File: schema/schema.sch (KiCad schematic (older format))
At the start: 10 parts, among them J1 Conn_01x04_Male, J2 Conn_01x04_Male, J3 Conn_01x05_Male

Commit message: Update PCB
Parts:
- C2, C4: footprint Capacitors_THT:CP_Radial_D5.0mm_P2.50mm -> Capacitor_THT:CP_Radial_D8.0mm_P5.00mm
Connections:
- wire segments 81 -> 75
- no-connect marks 0 -> 62
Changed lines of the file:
@@
 $EndDescr
-$Comp
-L schema-rescue:ARDUINO_MEGA-shield_arduino-test-rescue SH1
-U 1 1 5E01C684
-P 3250 3800
-F 0 "SH1" H 3262 6593 60  0000 C CNN
-F 1 "ARDUINO_MEGA" H 3262 6487 60  0000 C CNN
-F 2 "SHIELD_ARDUINO:ARDUINO_MEGA_2560_R3_ELL" H 2300 4100 60  0001 C CNN
-F 3 "http://arduino.cc/en/Main/ArduinoBoardMega2560" H 3262 6381 60  0000 C CNN
-	1    3250 3800
-	1    0    0    -1
-$EndComp
 $Comp
 L Driver_Motor:Pololu_Breakout_A4988 A1
@@
 	7000 1550 7200 1550
 Wire Wire Line
-	7200 1850 7000 1850
-Wire Wire Line
-	7000 1950 7200 1950
-Wire Wire Line
 	7200 2050 7000 2050
-Wire Wire Line
-	7000 2250 7200 2250
-Wire Wire Line
-	7200 2350 7000 2350
 Wire Wire Line
 	7000 2450 7200 2450
@@
 	4700 2500 4800 2400
 Wire Wire Line
-	4400 2500 4425 2500
-Connection ~ 4425 2500
-Wire Wire Line
-	4425 2500 4700 2500
-Wire Wire Line
-	4400 2300 4425 2300
-Connection ~ 4425 2300
-Wire Wire Line
-	4425 2300 4700 2300
-Wire Wire Line
-	4400 2200 4425 2200
-Connection ~ 4425 2200
-Wire Wire Line
-	4425 2200 4700 2200
-Wire Wire Line
-	4400 2100 4425 2100
-Connection ~ 4425 2100
-Wire Wire Line
-	4425 2100 4700 2100
-Wire Wire Line
-	4400 2000 4425 2000
-Connection ~ 4425 2000
-Wire Wire Line
-	4425 2000 4700 2000
-Wire Wire Line
-	4400 1800 4425 1800
-Connection ~ 4425 1800
-Wire Wire Line
 	4425 1800 4700 1800
-Wire Wire Line
-	4400 1900 4425 1900
-Connection ~ 4425 1900
 Wire Wire Line
 	4425 1900 4700 1900
@@
 	0    -1   -1   0
 $EndComp
-Connection ~ 2100 2200
 Wire Wire Line
 	1550 2000 2100 2000
@@
 F 0 "C2" H 8388 1446 50  0000 L CNN
 F 1 "100u" H 8388 1355 50  0000 L CNN
-F 2 "Capacitors_THT:CP_Radial_D5.0mm_P2.50mm" H 8300 1400 50  0001 C CNN
+F 2 "Capacitor_THT:CP_Radial_D8.0mm_P5.00mm" H 8300 1400 50  0001 C CNN
 F 3 "~" H 8300 1400 50  0001 C CNN
 	1    8300 1400
@@
 F 0 "C4" H 8488 4196 50  0000 L CNN
 F 1 "100u" H 8488 4105 50  0000 L CNN
-F 2 "Capacitors_THT:CP_Radial_D5.0mm_P2.50mm" H 8400 4150 50  0001 C CNN
+F 2 "Capacitor_THT:CP_Radial_D8.0mm_P5.00mm" H 8400 4150 50  0001 C CNN
 F 3 "~" H 8400 4150 50  0001 C CNN
 	1    8400 4150
@@
 Wire Wire Line
 	4650 5550 5850 5550
+NoConn ~ 2100 4300
+NoConn ~ 2100 4400
+NoConn ~ 2100 5075
+NoConn ~ 2100 4875
+NoConn ~ 2100 4775
+NoConn ~ 2100 4675
+NoConn ~ 2100 4575
+NoConn ~ 2100 5175
+NoConn ~ 2100 5275
+NoConn ~ 2100 5375
+NoConn ~ 2100 5475
+NoConn ~ 2100 5575
+NoConn ~ 2100 5675
+NoConn ~ 2100 5775
+NoConn ~ 2100 5975
+NoConn ~ 2100 6075
+NoConn ~ 2100 6175
+NoConn ~ 2100 6275
+NoConn ~ 4425 6150
+NoConn ~ 4425 6050
+NoConn ~ 4425 5850
+NoConn ~ 4425 5750
+NoConn ~ 4425 5650
+NoConn ~ 4425 5550
+NoConn ~ 4425 5450
+NoConn ~ 4425 5250
+NoConn ~ 4425 5150
+NoConn ~ 4425 5050
+NoConn ~ 4425 4950
+NoConn ~ 4425 4850
+NoConn ~ 4425 4750
+NoConn ~ 4425 4650
+NoConn ~ 4425 4550
+NoConn ~ 4425 4400
+NoConn ~ 4425 4300
+NoConn ~ 4425 4100
+NoConn ~ 4425 4000
+NoConn ~ 4425 3900
+NoConn ~ 4425 3800
+NoConn ~ 4425 3700
+NoConn ~ 4425 3600
+NoConn ~ 4425 3500
+NoConn ~ 4425 3400
+NoConn ~ 4425 3200
+NoConn ~ 4425 3100
+NoConn ~ 4425 2900
+NoConn ~ 4425 2800
+NoConn ~ 4425 2700
+NoConn ~ 4425 2600
+Wire Wire Line
+	4425 1700 4450 1700
+NoConn ~ 4425 1600
+NoConn ~ 4425 1500
+NoConn ~ 4425 1400
+Wire Wire Line
+	4425 2200 4700 2200
+Wire Wire Line
+	4425 2000 4700 2000
+Wire Wire Line
+	4425 2100 4700 2100
+Connection ~ 2100 2200
+Wire Wire Line
+	4425 2300 4700 2300
+Wire Wire Line
+	4425 2500 4700 2500
+Wire Wire Line
+	4425 3000 4650 3000
 Wire Wire Line
 	4400 3000 4425 3000
 Connection ~ 4425 3000
-Wire Wire Line
-	4425 3000 4650 3000
+$Comp
+L schema-rescue:ARDUINO_MEGA-shield_arduino-test-rescue SH1
+U 1 1 5E01C684
+P 3250 3800
+F 0 "SH1" H 3262 6593 60  0000 C CNN
+F 1 "ARDUINO_MEGA" H 3262 6487 60  0000 C CNN
+F 2 "SHIELD_ARDUINO:ARDUINO_MEGA_2560_R3_ELL" H 2300 4100 60  0001 C CNN
+F 3 "http://arduino.cc/en/Main/ArduinoBoardMega2560" H 3262 6381 60  0000 C CNN
+	1    3250 3800
+	1    0    0    -1
+$EndComp
+NoConn ~ 2100 1700
+NoConn ~ 2100 1800
+NoConn ~ 2100 1900
+NoConn ~ 2100 2700
+NoConn ~ 2100 2800
+NoConn ~ 2100 2900
+NoConn ~ 2100 3000
+NoConn ~ 2100 3100
+NoConn ~ 2100 3200
+NoConn ~ 7200 1650
+Wire Wire Line
+	7000 2250 7200 2250
+Wire Wire Line
+	7000 2350 7200 2350
+Wire Wire Line
+	7200 1850 7000 1850
+Wire Wire Line
+	7200 1950 7000 1950
 Wire Bus Line
 	4800 1700 4800 3850

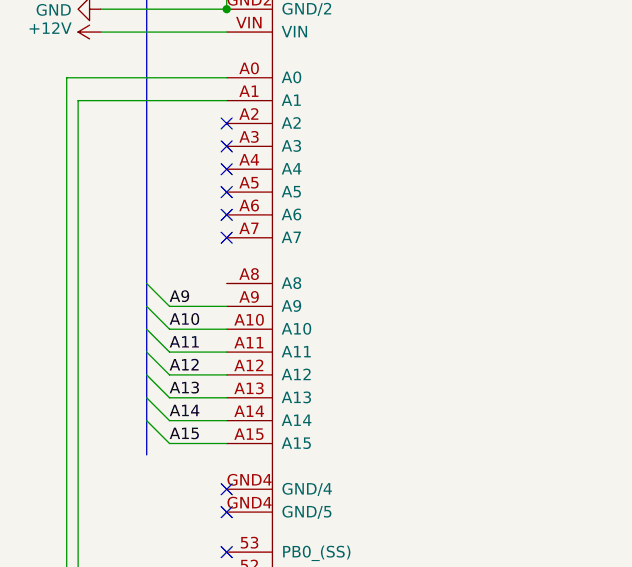
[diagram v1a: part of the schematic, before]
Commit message: Deplacement des trous
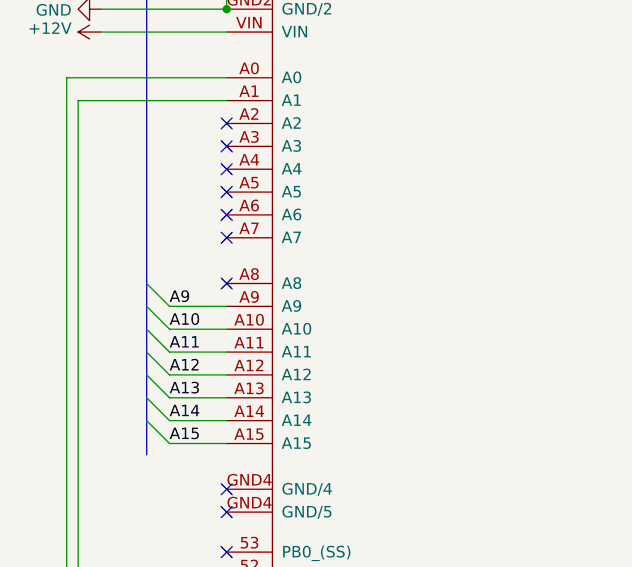
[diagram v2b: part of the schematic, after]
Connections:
- no-connect marks 62 -> 63
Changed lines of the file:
@@
 Wire Wire Line
 	7200 1950 7000 1950
+NoConn ~ 2100 3400
 Wire Bus Line
 	4800 1700 4800 3850

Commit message: Modifiction du condo de 100nF
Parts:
- C1, C3: footprint Capacitors_THT:C_Disc_D3.0mm_W1.6mm_P2.50mm -> Capacitor_THT:C_Disc_D5.1mm_W3.2mm_P5.00mm
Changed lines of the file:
@@
 F 0 "C1" H 7412 904 50  0000 R CNN
 F 1 "100n" H 7850 850 50  0000 R CNN
-F 2 "Capacitors_THT:C_Disc_D3.0mm_W1.6mm_P2.50mm" H 7500 950 50  0001 C CNN
+F 2 "Capacitor_THT:C_Disc_D5.1mm_W3.2mm_P5.00mm" H 7500 950 50  0001 C CNN
 F 3 "~" H 7500 950 50  0001 C CNN
 	1    7500 950
@@
 F 0 "C3" H 7462 3704 50  0000 R CNN
 F 1 "100n" H 7900 3650 50  0000 R CNN
-F 2 "Capacitors_THT:C_Disc_D3.0mm_W1.6mm_P2.50mm" H 7550 3750 50  0001 C CNN
+F 2 "Capacitor_THT:C_Disc_D5.1mm_W3.2mm_P5.00mm" H 7550 3750 50  0001 C CNN
 F 3 "~" H 7550 3750 50  0001 C CNN
 	1    7550 3750

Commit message: Modificatin pour la 3D sur les connexteurs JST
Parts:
- J1, J2: footprint Connectors_JST:JST_XH_B04B-XH-A_04x2.50mm_Straight -> Connector_JST:JST_XH_B4B-XH-A_1x04_P2.50mm_Vertical
- J3: footprint Connectors_JST:JST_XH_B05B-XH-A_05x2.50mm_Straight -> Connector_JST:JST_XH_B5B-XH-A_1x05_P2.50mm_Vertical
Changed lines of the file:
@@
 F 0 "J1" H 9072 1932 50  0000 R CNN
 F 1 "Conn_01x04_Male" H 9072 2023 50  0000 R CNN
-F 2 "Connectors_JST:JST_XH_B04B-XH-A_04x2.50mm_Straight" H 9100 2050 50  0001 C CNN
+F 2 "Connector_JST:JST_XH_B4B-XH-A_1x04_P2.50mm_Vertical" H 9100 2050 50  0001 C CNN
 F 3 "~" H 9100 2050 50  0001 C CNN
 	1    9100 2050
@@
 F 0 "J2" H 9122 4682 50  0000 R CNN
 F 1 "Conn_01x04_Male" H 9122 4773 50  0000 R CNN
-F 2 "Connectors_JST:JST_XH_B04B-XH-A_04x2.50mm_Straight" H 9150 4800 50  0001 C CNN
+F 2 "Connector_JST:JST_XH_B4B-XH-A_1x04_P2.50mm_Vertical" H 9150 4800 50  0001 C CNN
 F 3 "~" H 9150 4800 50  0001 C CNN
 	1    9150 4800
@@
 F 0 "J3" H 6022 5682 50  0000 R CNN
 F 1 "Conn_01x05_Male" H 6022 5773 50  0000 R CNN
-F 2 "Connectors_JST:JST_XH_B05B-XH-A_05x2.50mm_Straight" H 6050 5750 50  0001 C CNN
+F 2 "Connector_JST:JST_XH_B5B-XH-A_1x05_P2.50mm_Vertical" H 6050 5750 50  0001 C CNN
 F 3 "~" H 6050 5750 50  0001 C CNN
 	1    6050 5750
